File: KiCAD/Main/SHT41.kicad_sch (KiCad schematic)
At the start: 4 parts, among them U17 SHT4x

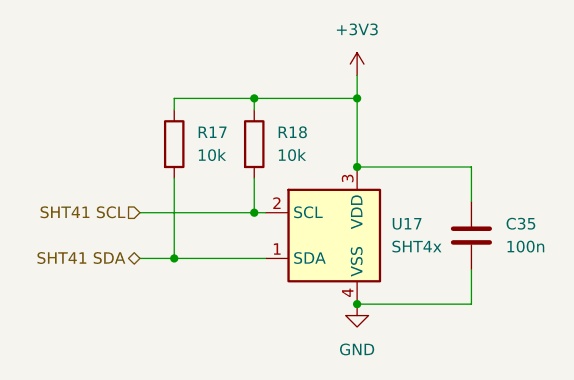
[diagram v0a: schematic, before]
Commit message: save after realizing branch was not switched to layoutv2
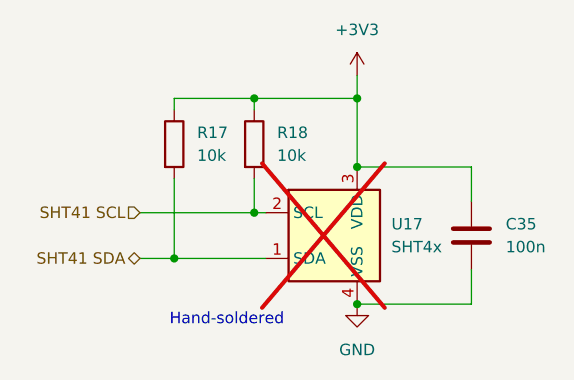
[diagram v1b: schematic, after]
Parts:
- U17: now not fitted; now left out of the parts list
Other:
- note added: "Hand-soldered"
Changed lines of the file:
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@@
 	(generator_version "9.0")
 	(paper "A4")
+	(text "Hand-soldered"
+		(exclude_from_sim no)
+		(at 112.522 93.218 0)
+		(effects
+			(font
+				(size 1.27 1.27)
+			)
+		)
+	)
 	(junction
 		(at 127 76.2)
@@
 		(unit 1)
 		(exclude_from_sim no)
-		(in_bom yes)
+		(in_bom no)
 		(on_board yes)
-		(dnp no)
+		(dnp yes)
 		(fields_autoplaced yes)
 		(property "Reference" "U17"
